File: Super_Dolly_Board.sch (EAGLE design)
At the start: 106 parts, among them J1 10118193-0001LF, J3 SJ1-2503A, J4 RJHSE-5381, J5 SJ1-2503A, J6 SJ1-2503A, P1 TC33X-2, SW1 SKQUDBE010, U1 AT90USB646-MU, U10 IP4234CZ6, U11 AT90USB646-AU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

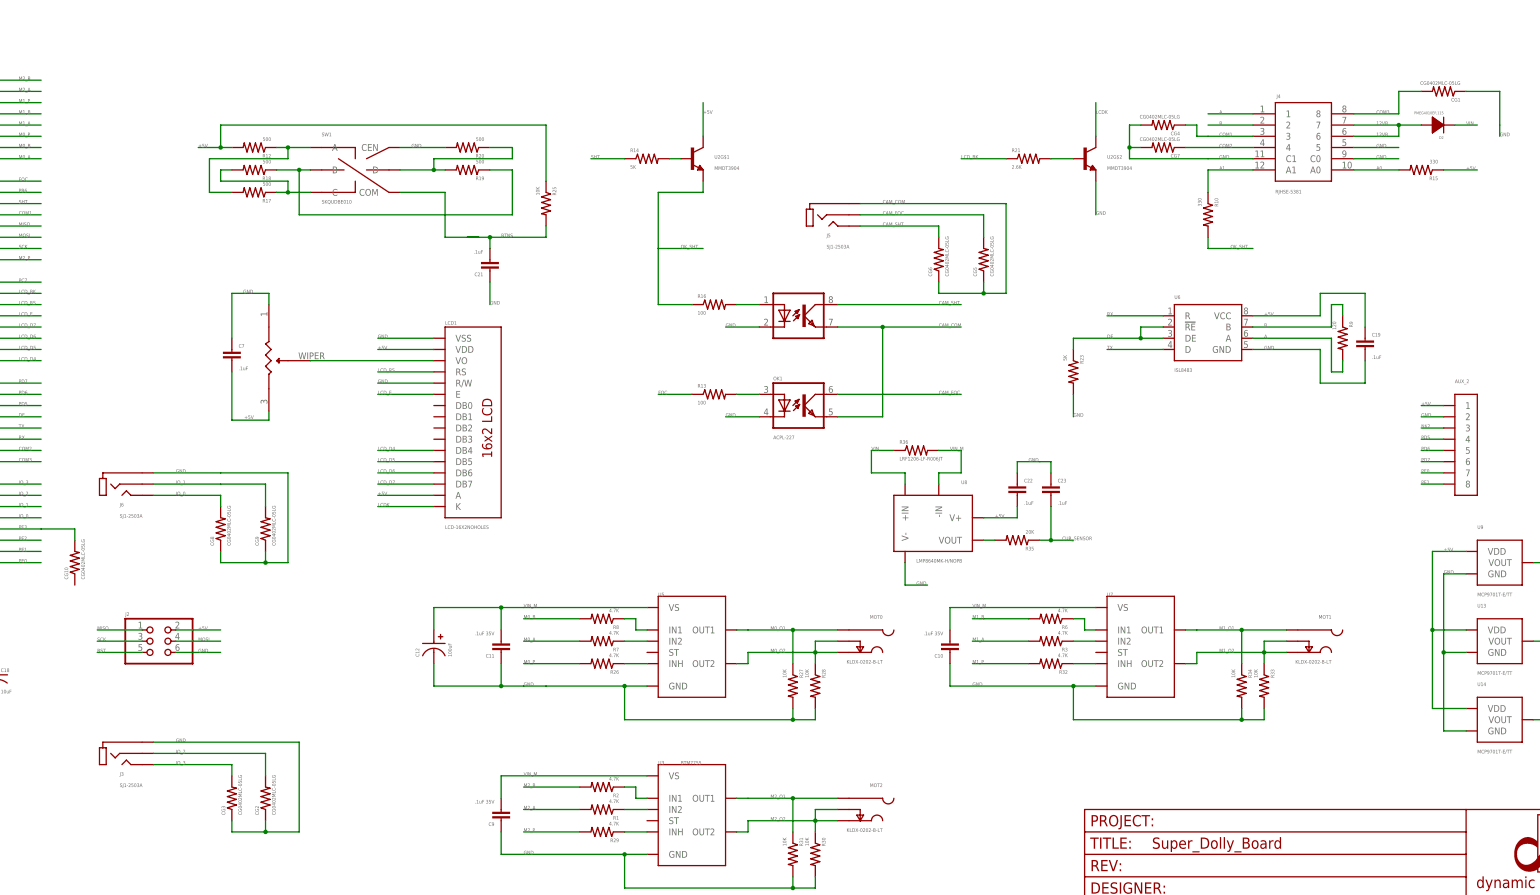
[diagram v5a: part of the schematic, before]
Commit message: changed ESD protection to TPD1E10B06DPYR
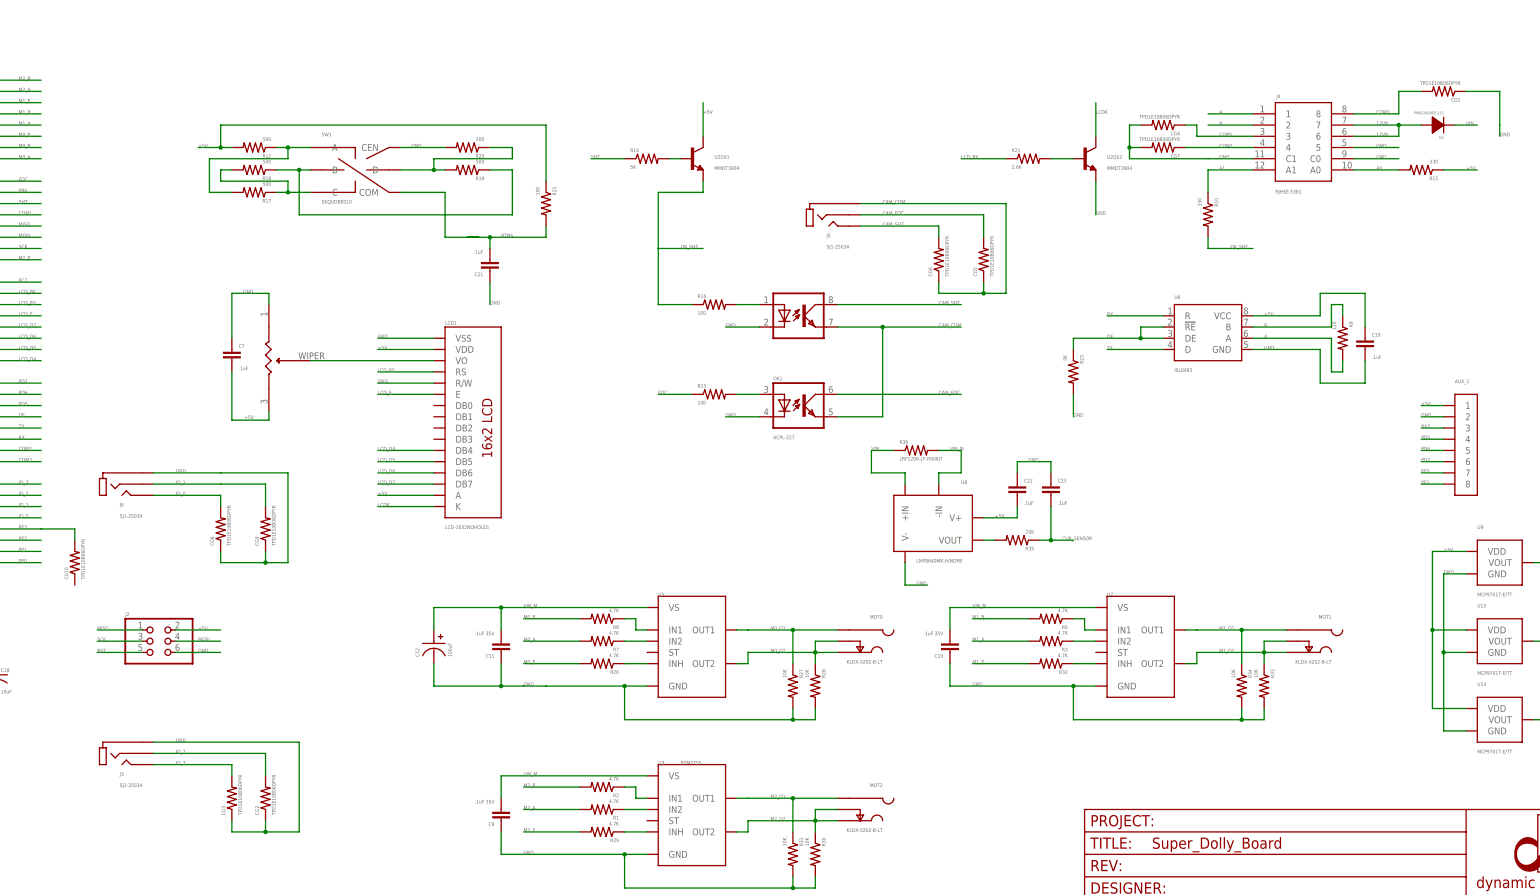
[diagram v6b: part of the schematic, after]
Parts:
- CG1, CG10, CG2, CG3, CG4, CG5, CG6, CG7, CG8, CG9: value CG0402MLC-05LG -> TPD1E10B06DPYR
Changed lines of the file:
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@@
 <part name="J2" library="parkers_parts" deviceset="P2X03" device=""/>
 <part name="J3" library="parkers_parts" deviceset="TRS_STEREO_JACK" device="SJ1-2503A" value="SJ1-2503A"/>
-<part name="CG2" library="parkers_parts" deviceset="RESISTOR" device="0402" value="CG0402MLC-05LG"/>
-<part name="CG3" library="parkers_parts" deviceset="RESISTOR" device="0402" value="CG0402MLC-05LG"/>
+<part name="CG2" library="parkers_parts" deviceset="RESISTOR" device="0402" value="TPD1E10B06DPYR"/>
+<part name="CG3" library="parkers_parts" deviceset="RESISTOR" device="0402" value="TPD1E10B06DPYR"/>
 <part name="MOT0" library="PP_Connectors" deviceset="DC_JACK" device="PTH_TIGHT" value="KLDX-0202-B-LT"/>
 <part name="MOT1" library="PP_Connectors" deviceset="DC_JACK" device="PTH_TIGHT" value="KLDX-0202-B-LT"/>
@@
 <part name="LOGO3" library="parkers_parts" deviceset="DP_LOGO" device="SUPERDOLLYBOARDLOGO"/>
 <part name="C21" library="parkers_parts" deviceset="CAP_NONPOL" device="0402" value=".1uF"/>
-<part name="CG5" library="parkers_parts" deviceset="RESISTOR" device="0402" value="CG0402MLC-05LG"/>
-<part name="CG6" library="parkers_parts" deviceset="RESISTOR" device="0402" value="CG0402MLC-05LG"/>
+<part name="CG5" library="parkers_parts" deviceset="RESISTOR" device="0402" value="TPD1E10B06DPYR"/>
+<part name="CG6" library="parkers_parts" deviceset="RESISTOR" device="0402" value="TPD1E10B06DPYR"/>
 <part name="R23" library="parkers_parts" deviceset="RESISTOR" device="0402" value="5K"/>
 <part name="U11" library="at90usb" deviceset="AT90USB647-*" device="AU" value="AT90USB646-AU"/>
@@
 <part name="U1" library="at90usb" deviceset="AT90USB647-*" device="MU" value="AT90USB646-MU"/>
 <part name="D2" library="parkers_parts" deviceset="DIODE" device="SOD-128" value="PMEG4010EP,115"/>
-<part name="CG4" library="parkers_parts" deviceset="RESISTOR" device="0402" value="CG0402MLC-05LG"/>
-<part name="CG7" library="parkers_parts" deviceset="RESISTOR" device="0402" value="CG0402MLC-05LG"/>
+<part name="CG4" library="parkers_parts" deviceset="RESISTOR" device="0402" value="TPD1E10B06DPYR"/>
+<part name="CG7" library="parkers_parts" deviceset="RESISTOR" device="0402" value="TPD1E10B06DPYR"/>
 <part name="U10" library="parkers_parts" deviceset="IP4234CZ6" device="SOT-457" value="IP4234CZ6"/>
-<part name="CG1" library="parkers_parts" deviceset="RESISTOR" device="0402" value="CG0402MLC-05LG"/>
+<part name="CG1" library="parkers_parts" deviceset="RESISTOR" device="0402" value="TPD1E10B06DPYR"/>
 <part name="C14" library="parkers_parts" deviceset="CAP_NONPOL" device="0402" value=".1uF"/>
 <part name="J6" library="parkers_parts" deviceset="TRS_STEREO_JACK" device="SJ1-2503A" value="SJ1-2503A"/>
-<part name="CG8" library="parkers_parts" deviceset="RESISTOR" device="0402" value="CG0402MLC-05LG"/>
-<part name="CG9" library="parkers_parts" deviceset="RESISTOR" device="0402" value="CG0402MLC-05LG"/>
+<part name="CG8" library="parkers_parts" deviceset="RESISTOR" device="0402" value="TPD1E10B06DPYR"/>
+<part name="CG9" library="parkers_parts" deviceset="RESISTOR" device="0402" value="TPD1E10B06DPYR"/>
 <part name="C12" library="PP_Passives" deviceset="CAPACITOR_POLARIZED" device="6.3MM_SMD" value="100uF"/>
 <part name="R25" library="parkers_parts" deviceset="RESISTOR" device="0402" value="10K"/>
@@
 <part name="R33" library="PP_Passives" deviceset="RESISTOR" device="0805" value="10K"/>
 <part name="R34" library="PP_Passives" deviceset="RESISTOR" device="0805" value="10K"/>
-<part name="CG10" library="parkers_parts" deviceset="RESISTOR" device="0402" value="CG0402MLC-05LG"/>
+<part name="CG10" library="parkers_parts" deviceset="RESISTOR" device="0402" value="TPD1E10B06DPYR"/>
 <part name="AUX_2" library="PP_Connectors" deviceset="PH_1X08" device="1.27MM_PTH"/>
 <part name="U8" library="PP_AnalogIC" deviceset="LMP8640" device="TSOT-6" value="LMP8640MK-H/NOPB"/>

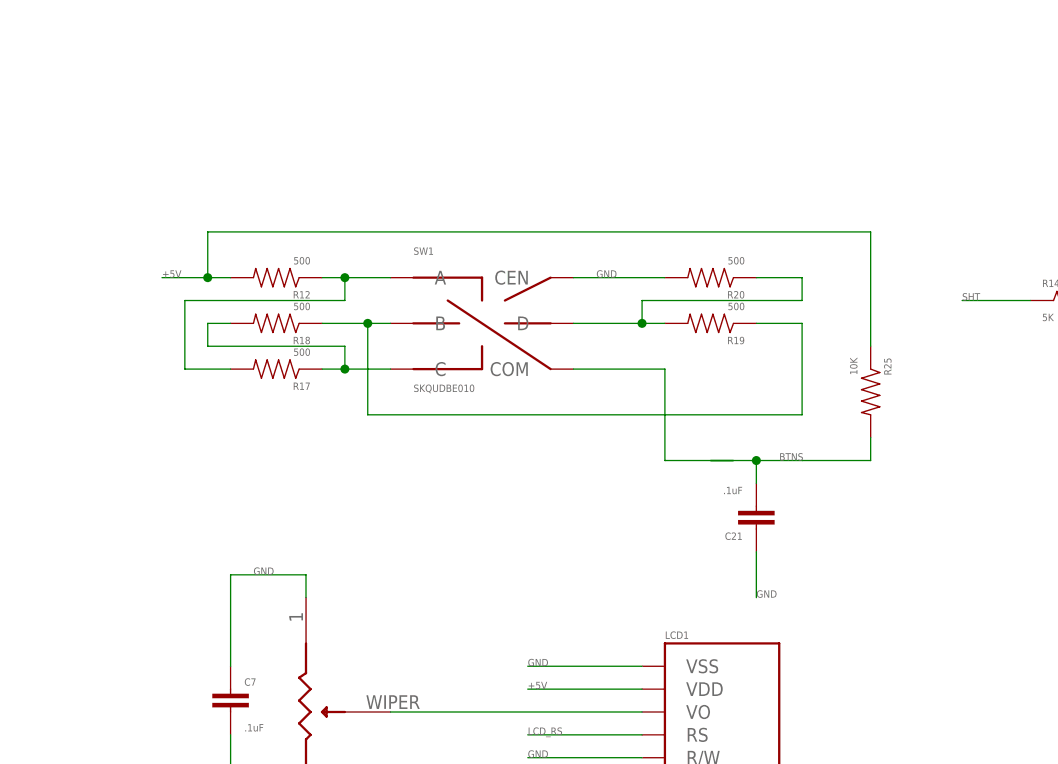
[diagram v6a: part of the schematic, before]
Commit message: added input board
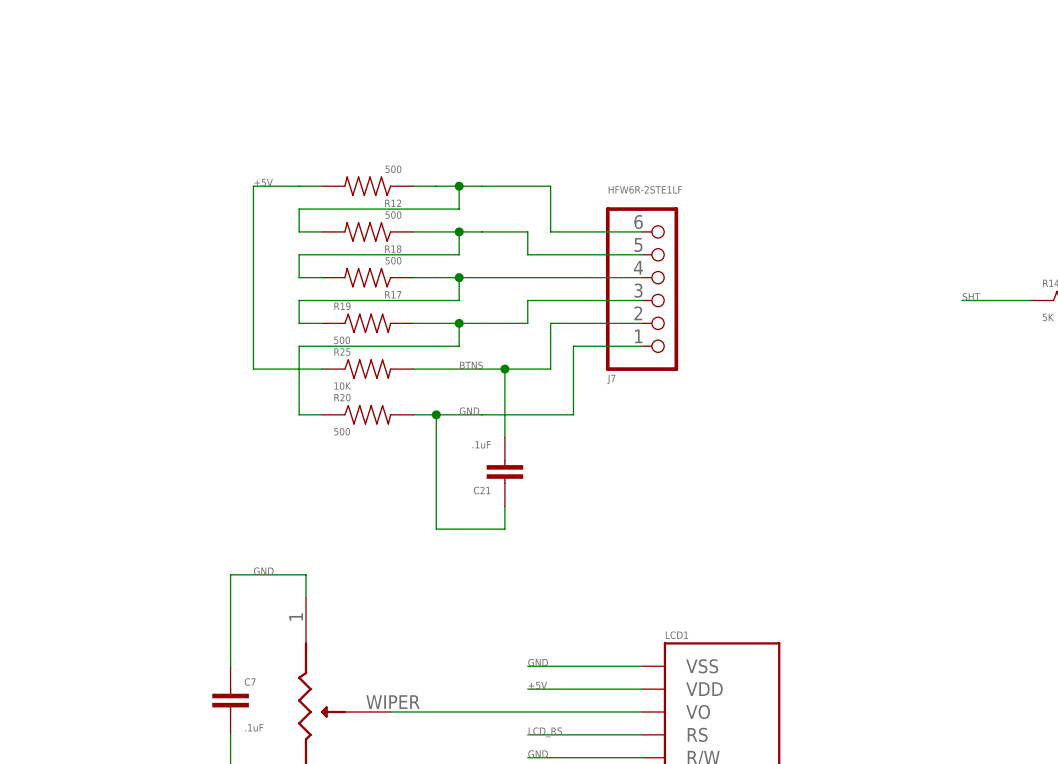
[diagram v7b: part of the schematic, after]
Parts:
- removed SW1: SKQUDBE010, parkers_parts:APLS_SKQ_MDSSMD
- added J7: HFW6R-2STE1LF, PP_Connectors:PH_1X06FFC
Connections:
- net BTNS: now also J7.2; no longer SW1.COM
- net GND: now also J7.1; no longer SW1.CEN
- net N$27: now also J7.6, R18.2; no longer R17.2, SW1.A
- net N$28: now also J7.4, R19.1; no longer R18.2, SW1.C
- net N$29: now also J7.5, R17.2; no longer R19.1, SW1.B
- net N$30: now also J7.3; no longer SW1.D
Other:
- moved on the sheet: C21, R12, R17, R18, R19, R20, R25

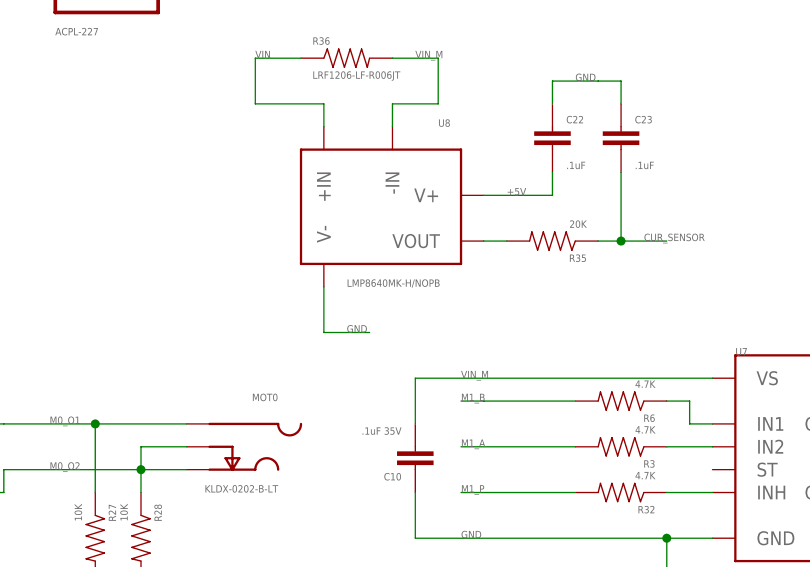
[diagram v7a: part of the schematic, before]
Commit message: fixed a part number issue
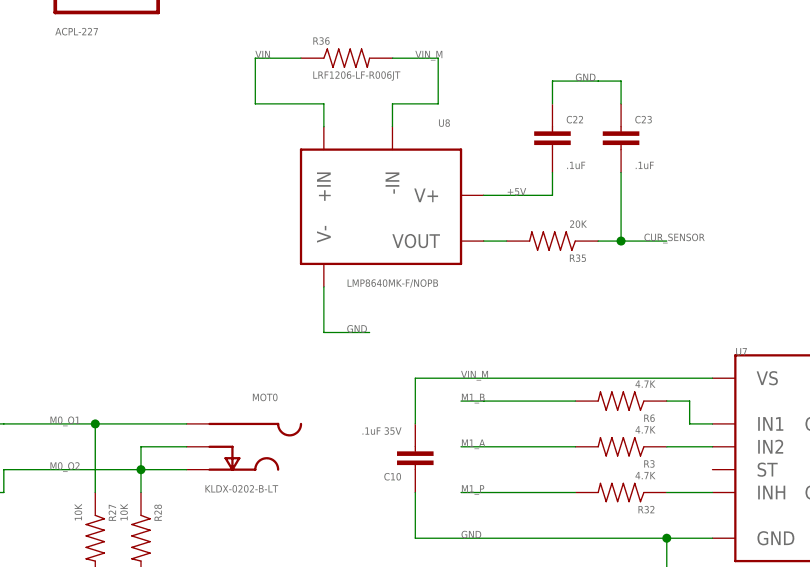
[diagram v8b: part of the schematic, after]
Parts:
- U8: value LMP8640MK-H/NOPB -> LMP8640MK-F/NOPB
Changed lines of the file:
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@@
 <part name="CG10" library="parkers_parts" deviceset="RESISTOR" device="0402" value="TPD1E10B06DPYR"/>
 <part name="AUX_2" library="PP_Connectors" deviceset="PH_1X08" device="1.27MM_PTH"/>
-<part name="U8" library="PP_AnalogIC" deviceset="LMP8640" device="TSOT-6" value="LMP8640MK-H/NOPB"/>
+<part name="U8" library="PP_AnalogIC" deviceset="LMP8640" device="TSOT-6" value="LMP8640MK-F/NOPB"/>
 <part name="C22" library="parkers_parts" deviceset="CAP_NONPOL" device="0402" value=".1uF"/>
 <part name="R35" library="parkers_parts" deviceset="RESISTOR" device="0402" value="20K"/>
